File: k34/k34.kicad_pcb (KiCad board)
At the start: 2 copper layers, 254.2 x 118.9 mm, 73 parts, among them U1 nice_nano

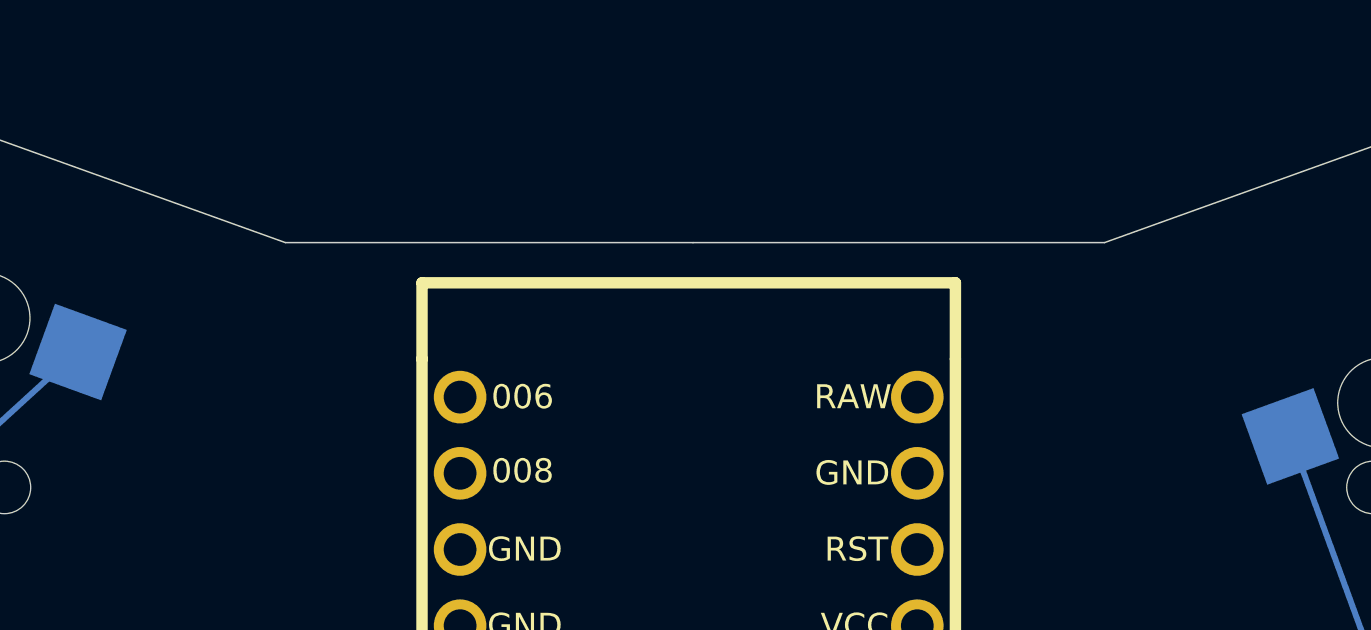
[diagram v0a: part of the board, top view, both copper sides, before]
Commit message: added plate pcb
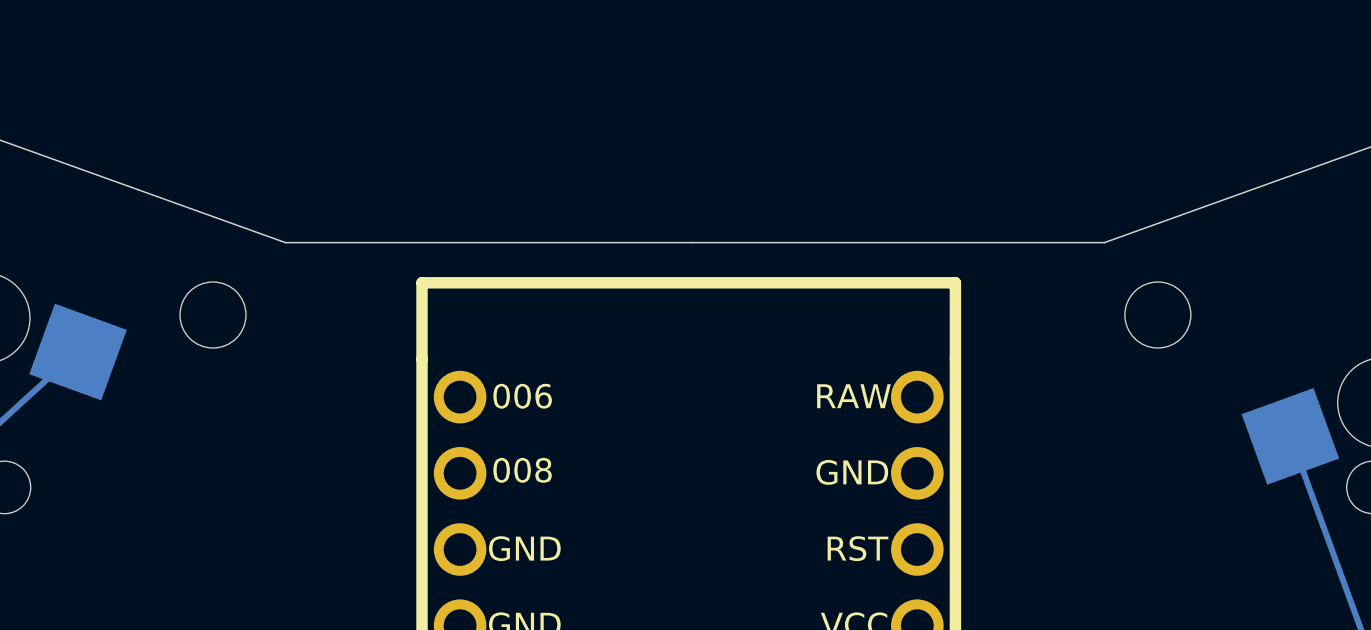
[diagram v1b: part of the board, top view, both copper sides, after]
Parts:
- added left_screw: MountingHole_2.2mm_M2, MountingHole:MountingHole_2.2mm_M2, F.Cu at (123.7, 58.3)
- added right_screw: MountingHole_2.2mm_M2, MountingHole:MountingHole_2.2mm_M2, F.Cu at (155.2, 58.3)
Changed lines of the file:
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@@
     (tracks 304)
     (zones 0)
-    (modules 73)
+    (modules 75)
     (nets 62)
   )
   (page A4)
   (layers
-    (0 F.Cu signal)
-    (31 B.Cu signal)
+    (0 F.Cu signal hide)
+    (31 B.Cu signal hide)
     (32 B.Adhes user hide)
     (33 F.Adhes user hide)
-    (34 B.Paste user)
-    (35 F.Paste user)
-    (36 B.SilkS user)
-    (37 F.SilkS user)
-    (38 B.Mask user)
+    (34 B.Paste user hide)
+    (35 F.Paste user hide)
+    (36 B.SilkS user hide)
+    (37 F.SilkS user hide)
+    (38 B.Mask user hide)
     (39 F.Mask user)
     (40 Dwgs.User user)
@@
     (44 Edge.Cuts user)
     (45 Margin user hide)
-    (46 B.CrtYd user)
-    (47 F.CrtYd user)
+    (46 B.CrtYd user hide)
+    (47 F.CrtYd user hide)
     (48 B.Fab user hide)
     (49 F.Fab user hide)
@@
     (visible_elements FFFFFF7F)
     (pcbplotparams
-      (layerselection 0x010fc_ffffffff)
+      (layerselection 0x01100_7ffffffe)
       (usegerberextensions false)
       (usegerberattributes true)
@@
       (padsonsilk false)
       (subtractmaskfromsilk false)
-      (outputformat 1)
+      (outputformat 5)
       (mirror false)
       (drillshape 0)
       (scaleselection 1)
-      (outputdirectory "gerbers/"))
+      (outputdirectory "plates/"))
   )
   (net 0 "")
@@
   )
   (module MountingHole:MountingHole_2.2mm_M2 (layer F.Cu)
+    (at 155.194 58.293)
+    (descr "Mounting Hole 2.2mm, no annular, M2")
+    (tags "mounting hole 2.2mm no annular m2")
+    (attr virtual)
+    (fp_text reference right_screw (at 0 -3.2) (layer F.Fab)
+      (effects (font (size 1 1) (thickness 0.15)))
+    )
+    (fp_text value MountingHole_2.2mm_M2 (at 0 3.2) (layer F.Fab)
+      (effects (font (size 1 1) (thickness 0.15)))
+    )
+    (fp_circle (center 0 0) (end 2.45 0) (layer F.CrtYd) (width 0.05))
+    (fp_circle (center 0 0) (end 2.2 0) (layer Cmts.User) (width 0.15))
+    (fp_text user %R (at 0.3 0) (layer F.Fab)
+      (effects (font (size 1 1) (thickness 0.15)))
+    )
+    (pad 1 np_thru_hole circle (at 0 0) (size 2.2 2.2) (drill 2.2) (layers *.Cu *.Mask))
+  )
+  (module MountingHole:MountingHole_2.2mm_M2 (layer F.Cu)
+    (at 123.698 58.293)
+    (descr "Mounting Hole 2.2mm, no annular, M2")
+    (tags "mounting hole 2.2mm no annular m2")
+    (attr virtual)
+    (fp_text reference left_screw (at 0 -3.2) (layer F.Fab)
+      (effects (font (size 1 1) (thickness 0.15)))
+    )
+    (fp_text value MountingHole_2.2mm_M2 (at 0 3.2) (layer F.Fab)
+      (effects (font (size 1 1) (thickness 0.15)))
+    )
+    (fp_circle (center 0 0) (end 2.45 0) (layer F.CrtYd) (width 0.05))
+    (fp_circle (center 0 0) (end 2.2 0) (layer Cmts.User) (width 0.15))
+    (fp_text user %R (at 0.3 0) (layer F.Fab)
+      (effects (font (size 1 1) (thickness 0.15)))
+    )
+    (pad 1 np_thru_hole circle (at 0 0) (size 2.2 2.2) (drill 2.2) (layers *.Cu *.Mask))
+  )
+  (module MountingHole:MountingHole_2.2mm_M2 (layer F.Cu)

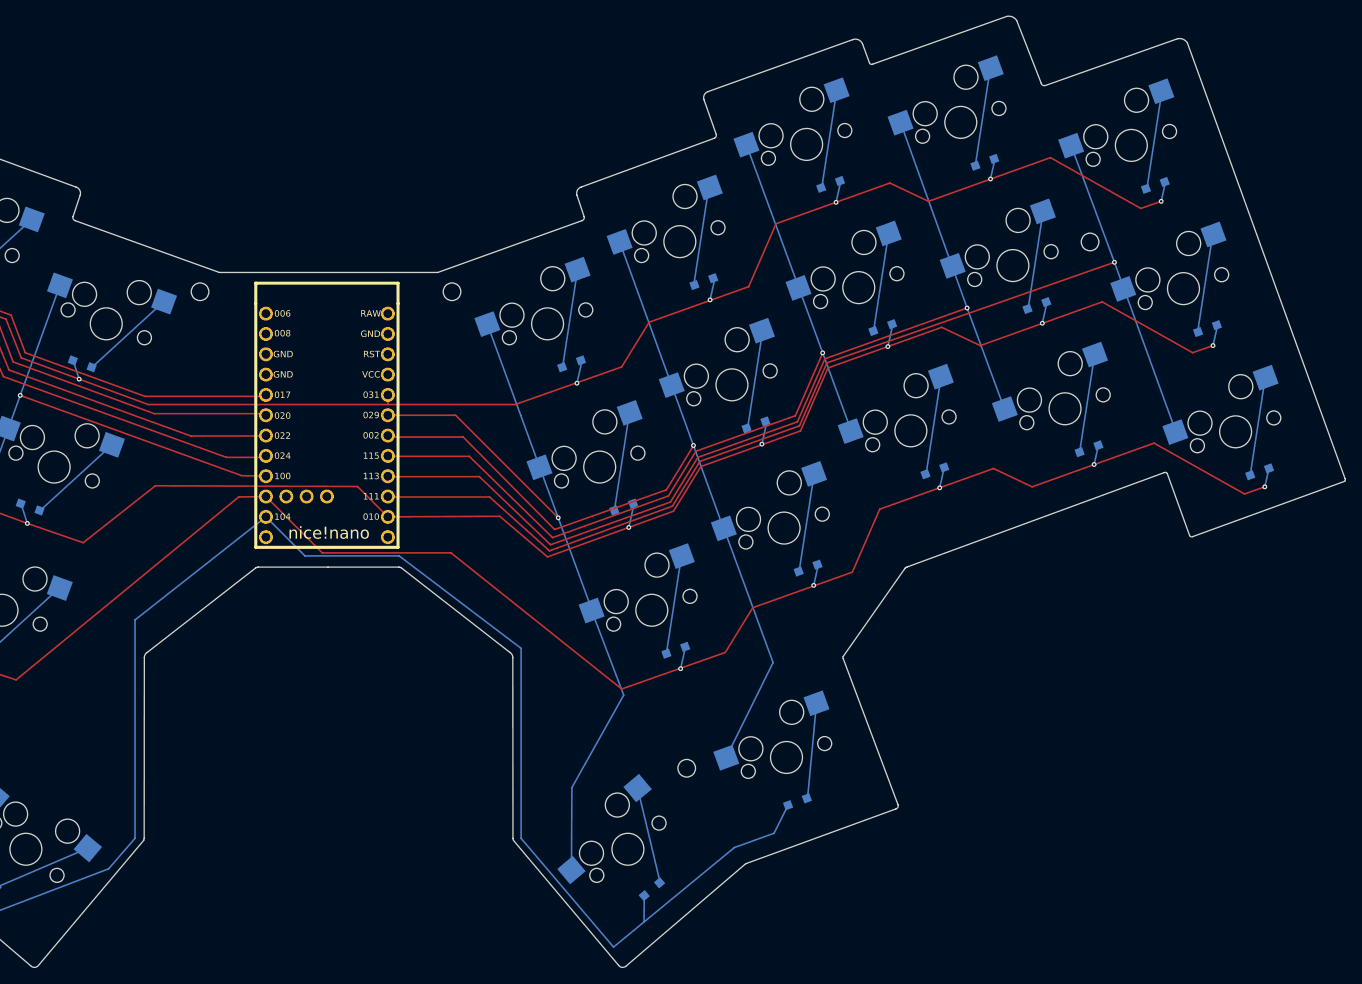
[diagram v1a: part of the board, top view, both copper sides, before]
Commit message: added 3rd screw
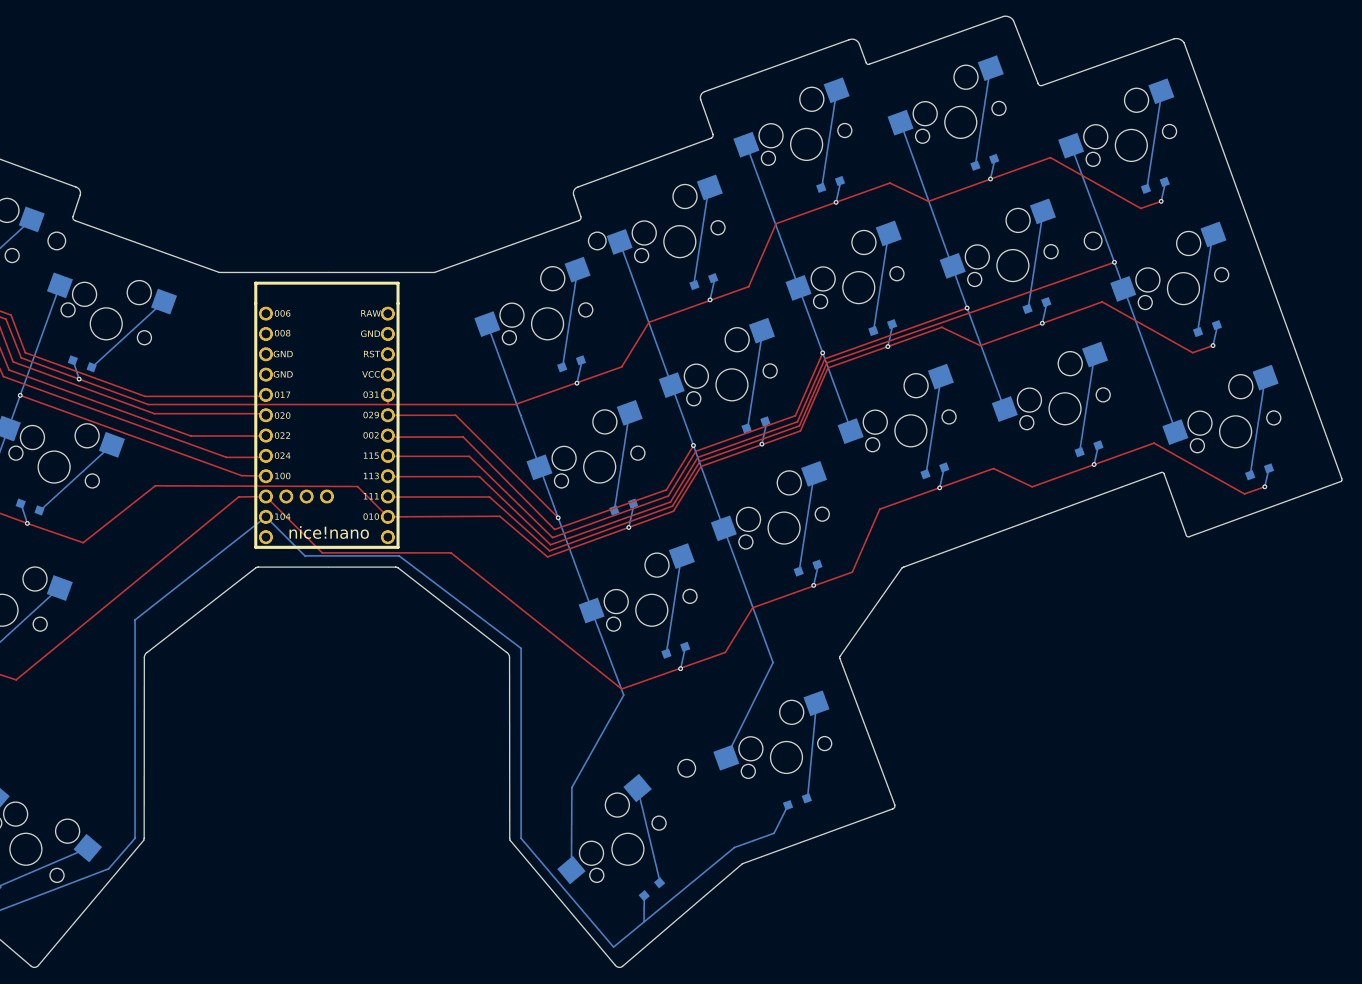
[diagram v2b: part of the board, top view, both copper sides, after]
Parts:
- removed the right_screw at (155.2, 58.3)
- removed the right_screw at (234.9, 52.1)
- added left_screw: MountingHole_2.2mm_M2, MountingHole:MountingHole_2.2mm_M2, F.Cu at (105.8, 51.9)
- added right_screw: MountingHole_2.2mm_M2, MountingHole:MountingHole_2.2mm_M2, F.Cu at (235.3, 51.9)
- moved left_screw 50.1 mm to (173.4, 51.9)
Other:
- board size 254.2 x 118.9 mm -> 253.8 x 118.9 mm

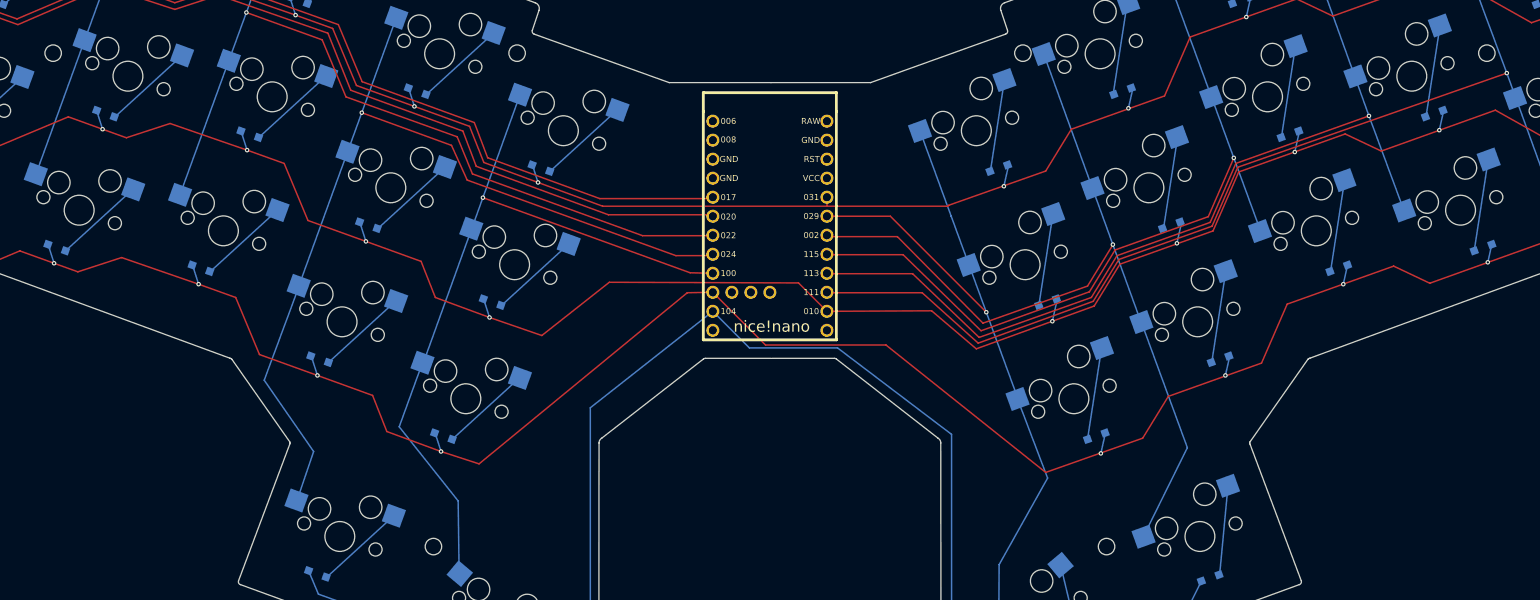
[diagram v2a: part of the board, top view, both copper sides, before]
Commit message: updated schematic with wider diode
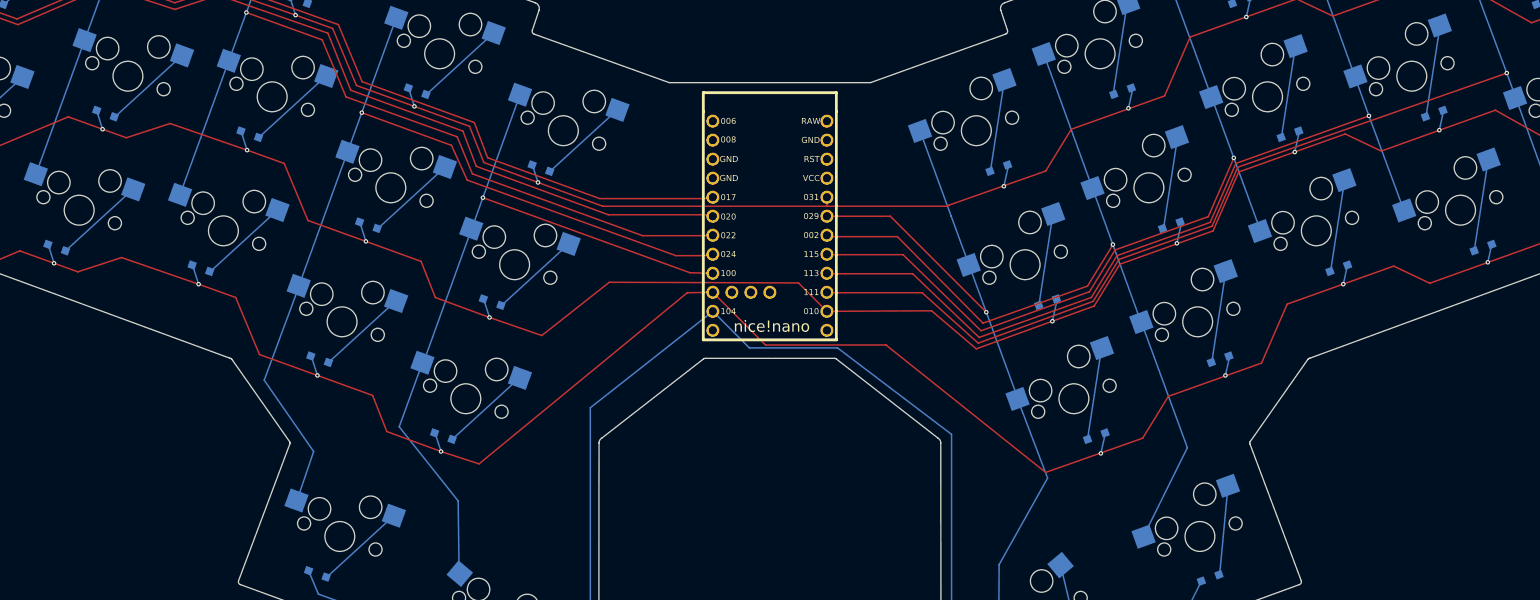
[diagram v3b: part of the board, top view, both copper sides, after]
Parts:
- removed left_screw (x3), left_screw_bot, right_screw, right_screw_bot: MountingHole_2.2mm_M2, MountingHole:MountingHole_2.2mm_M2

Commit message: save kicad pro
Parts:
- D1, D10, D11, D12, D13, D14, D15, D16, D17, D18, D19, D2, D20, D21, D22, D23, D24, D25, D26, D27, D28, D29, D3, D30, D31, D32, D33, D34, D4, D5, D6, D7, D8, D9: footprint Diode_SMD:D_SOD-323_HandSoldering -> Diode_SMD:D_SOD-128
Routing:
- net /row1: track 279.3 -> 285.6 mm
- net /row2: track 303.0 -> 308.4 mm
- net /row0: track 261.7 -> 266.1 mm
- net Net-(D27-Pad2): track 12.2 -> 13.1 mm
- net /row3: track 207.9 -> 207.1 mm
- net Net-(D6-Pad2): track 12.2 -> 13.0 mm
- net Net-(D29-Pad2): track 12.2 -> 13.0 mm
- net Net-(D16-Pad2): track 12.2 -> 13.0 mm
- net Net-(D26-Pad2): track 12.2 -> 13.0 mm
- net Net-(D28-Pad2): track 12.2 -> 12.9 mm
- net Net-(D19-Pad2): track 12.2 -> 12.8 mm
- net Net-(D9-Pad2): track 12.2 -> 12.7 mm
- net Net-(D3-Pad2): track 12.2 -> 11.7 mm
- net Net-(D18-Pad2): track 12.2 -> 12.7 mm
- net Net-(D7-Pad2): track 12.2 -> 12.7 mm
